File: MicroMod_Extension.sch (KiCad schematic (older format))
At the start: 69 parts, among them J1 2199230-4, J2 XKB_U262-16XN-4BVC11, J3 RSP-122811-01, SW1 TL1014BF160QG, U1 24aa64ft-eot, U2 nRF51822-QFAA-R7, U3 RFX2411N, U4 TPS62170DSG, U5 NCP702SN30T1G, U6 NCP702SN30T1G, Y1 TSX-3225_16.0000MF18X-AC3

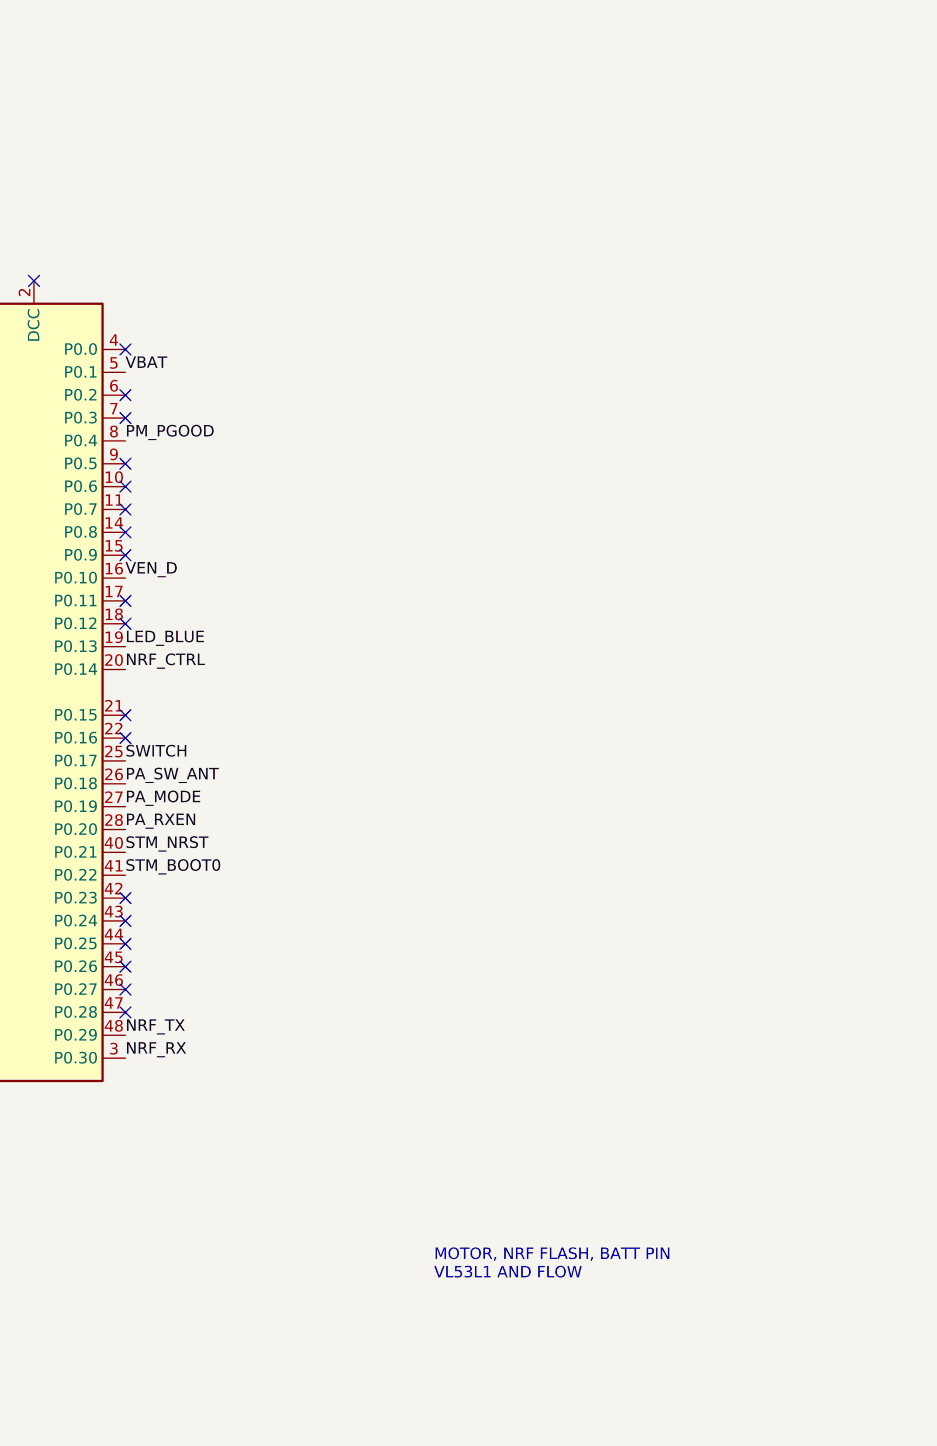
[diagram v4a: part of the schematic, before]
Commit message: add connector for esc and flow
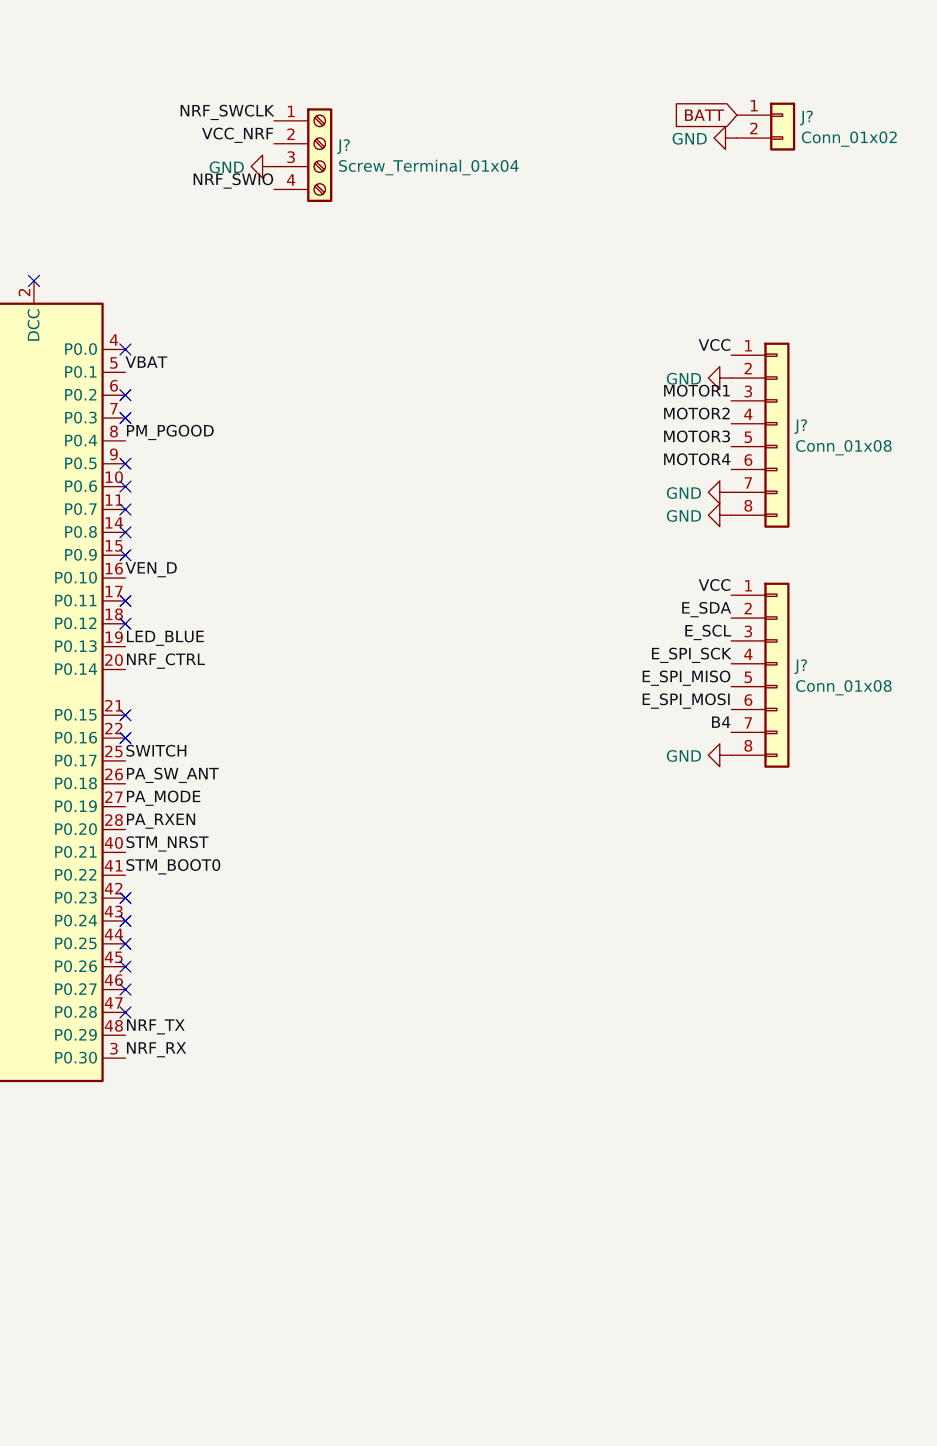
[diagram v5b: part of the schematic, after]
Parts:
- added J?: Screw_Terminal_01x04, Connector_PinHeader_2.54mm:PinHeader_1x04_P2.54mm_Vertical, symbol Connector:Screw_Terminal_01x04
- added J?: Conn_01x02, symbol Connector_Generic:Conn_01x02
- added J? (x2): Conn_01x08, MicroMod_Extension:JST_SUR_BM08B-SURS-TF_1x08-1MP_P0.80mm_Vertical, symbol Connector_Generic:Conn_01x08
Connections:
- net B4: now also J?.7 (Pin_7)
- net BATT: now also J?.1 (Pin_1)
- net E_SCL: now also J?.3 (Pin_3)
- net E_SDA: now also J?.2 (Pin_2)
- net E_SPI_MISO: now also J?.5 (Pin_5)
- net E_SPI_MOSI: now also J?.6 (Pin_6)
- net E_SPI_SCK: now also J?.4 (Pin_4)
- net GND: now also J?.2 (Pin_2), J?.2 (Pin_2), J?.3 (Pin_3), J?.7 (Pin_7), J?.8 (Pin_8), J?.8 (Pin_8)
- net MOTOR1: now also J?.3 (Pin_3)
- net MOTOR2: now also J?.4 (Pin_4)
- net MOTOR3: now also J?.5 (Pin_5)
- net MOTOR4: now also J?.6 (Pin_6)
- net NRF_SWCLK: now also J?.1 (Pin_1)
- net NRF_SWIO: now also J?.4 (Pin_4)
- net VCC: now also J?.1 (Pin_1), J?.1 (Pin_1)
- net VCC_NRF: now also J?.2 (Pin_2)
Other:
- note removed: "MOTOR, NRF FLASH, BATT PIN\nVL53L1 AND FLOW"
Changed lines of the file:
@@
 Text Label 10250 4525 2    50   ~ 0
 NRF_SWCLK
-$Comp
-L MicroMod_Extension:XKB_U262-16XN-4BVC11 J2
-U 1 1 617B133B
-P 1550 7950
-F 0 "J2" H 1583 9125 50  0000 C CNN
-F 1 "XKB_U262-16XN-4BVC11" H 1583 9034 50  0000 C CNN
-F 2 "Connector_USB:USB_C_Receptacle_XKB_U262-16XN-4BVC11" H 1580 7960 50  0001 C CNN
-F 3 "" H 1580 7960 50  0001 C CNN
-	1    1550 7950
-	1    0    0    -1
-$EndComp
-Wire Wire Line
-	2050 8650 2050 8750
 Wire Wire Line
 	2050 9000 1450 9000
-Connection ~ 2050 8750
-Wire Wire Line
-	2050 8750 2050 9000
 Connection ~ 2050 9000
-Connection ~ 2050 8050
-Connection ~ 2050 7800
 Wire Wire Line
 	2050 7200 2050 7300
@@
 Wire Wire Line
 	2150 7300 2050 7300
-Connection ~ 2050 8450
-Connection ~ 2050 7300
 NoConn ~ 2050 8250
 NoConn ~ 2050 8350
@@
 Wire Wire Line
 	2050 7000 2050 7100
-Connection ~ 2050 7000
 $Comp
 L MicroMod_Extension:2450BM14E0003T FL1
@@
 Wire Wire Line
 	2050 7200 2150 7200
-Connection ~ 2050 7200
 NoConn ~ 12050 4825
 NoConn ~ 12050 4725
@@
 	8500 5850 8500 5325
 Connection ~ 8500 5325
-Text Notes 13400 6000 0    50   ~ 0
- MOTOR, NRF FLASH, BATT PIN\nVL53L1 AND FLOW
+Connection ~ 2050 7200
+Connection ~ 2050 7000
+Connection ~ 2050 7300
+Connection ~ 2050 8450
+Connection ~ 2050 7800
+Connection ~ 2050 8050
+Connection ~ 2050 8750
+Wire Wire Line
+	2050 8750 2050 9000
+Wire Wire Line
+	2050 8650 2050 8750
+$Comp
+L MicroMod_Extension:XKB_U262-16XN-4BVC11 J2
+U 1 1 617B133B
+P 1550 7950
+F 0 "J2" H 1583 9125 50  0000 C CNN
+F 1 "XKB_U262-16XN-4BVC11" H 1583 9034 50  0000 C CNN
+F 2 "Connector_USB:USB_C_Receptacle_XKB_U262-16XN-4BVC11" H 1580 7960 50  0001 C CNN
+F 3 "" H 1580 7960 50  0001 C CNN
+	1    1550 7950
+	1    0    0    -1
+$EndComp
+$Comp
+L Connector:Screw_Terminal_01x04 J?
+U 1 1 6180CF84
+P 12900 1025
+F 0 "J?" H 12980 1017 50  0000 L CNN
+F 1 "Screw_Terminal_01x04" H 12980 926 50  0000 L CNN
+F 2 "Connector_PinHeader_2.54mm:PinHeader_1x04_P2.54mm_Vertical" H 12900 1025 50  0001 C CNN
+F 3 "~" H 12900 1025 50  0001 C CNN
+	1    12900 1025
+	1    0    0    -1
+$EndComp
+Text Label 12700 925  2    50   ~ 0
+NRF_SWCLK
+Text Label 12700 1225 2    50   ~ 0
+NRF_SWIO
+Text Label 12700 1025 2    50   ~ 0
+VCC_NRF
+$Comp
+L power:GND #PWR?
+U 1 1 61871AB2
+P 12700 1125
+F 0 "#PWR?" H 12700 875 50  0001 C CNN
+F 1 "GND" V 12705 997 50  0000 R CNN
+F 2 "" H 12700 1125 50  0001 C CNN
+F 3 "" H 12700 1125 50  0001 C CNN
+	1    12700 1125
+	0    1    1    0
+$EndComp
+$Comp
+L Connector_Generic:Conn_01x02 J?
+U 1 1 6189B41D
+P 14925 900
+F 0 "J?" H 15005 892 50  0000 L CNN
+F 1 "Conn_01x02" H 15005 801 50  0000 L CNN
+F 2 "" H 14925 900 50  0001 C CNN
+F 3 "~" H 14925 900 50  0001 C CNN
+	1    14925 900
+	1    0    0    -1
+$EndComp
+$Comp
+L power:GND #PWR?
+U 1 1 6189BE51
+P 14725 1000
+F 0 "#PWR?" H 14725 750 50  0001 C CNN
+F 1 "GND" V 14730 872 50  0000 R CNN
+F 2 "" H 14725 1000 50  0001 C CNN
+F 3 "" H 14725 1000 50  0001 C CNN
+	1    14725 1000
+	0    1    1    0
+$EndComp
+Text GLabel 14725 900  0    50   Input ~ 0
+BATT
+$Comp
+L Connector_Generic:Conn_01x08 J?
+U 1 1 6197BE2D
+P 14900 2250
+F 0 "J?" H 14980 2242 50  0000 L CNN
+F 1 "Conn_01x08" H 14980 2151 50  0000 L CNN
+F 2 "MicroMod_Extension:JST_SUR_BM08B-SURS-TF_1x08-1MP_P0.80mm_Vertical" H 14900 2250 50  0001 C CNN
+F 3 "~" H 14900 2250 50  0001 C CNN
+	1    14900 2250
+	1    0    0    -1
+$EndComp
+$Comp
+L Connector_Generic:Conn_01x08 J?
+U 1 1 6197CCB9
+P 14900 3300
+F 0 "J?" H 14980 3292 50  0000 L CNN
+F 1 "Conn_01x08" H 14980 3201 50  0000 L CNN
+F 2 "MicroMod_Extension:JST_SUR_BM08B-SURS-TF_1x08-1MP_P0.80mm_Vertical" H 14900 3300 50  0001 C CNN
+F 3 "~" H 14900 3300 50  0001 C CNN
+	1    14900 3300
+	1    0    0    -1
+$EndComp
+Text Label 14700 1950 2    50   ~ 0
+VCC
+Text Label 14700 3000 2    50   ~ 0
+VCC
+$Comp
+L power:GND #PWR?
+U 1 1 619F4806
+P 14700 2650
+F 0 "#PWR?" H 14700 2400 50  0001 C CNN
+F 1 "GND" V 14705 2522 50  0000 R CNN
+F 2 "" H 14700 2650 50  0001 C CNN
+F 3 "" H 14700 2650 50  0001 C CNN
+	1    14700 2650
+	0    1    1    0
+$EndComp
+$Comp
+L power:GND #PWR?
+U 1 1 61A085B5
+P 14700 3700
+F 0 "#PWR?" H 14700 3450 50  0001 C CNN
+F 1 "GND" V 14705 3572 50  0000 R CNN
+F 2 "" H 14700 3700 50  0001 C CNN
+F 3 "" H 14700 3700 50  0001 C CNN
+	1    14700 3700
+	0    1    1    0
+$EndComp
+Text Label 14700 2150 2    50   ~ 0
+MOTOR1
+Text Label 14700 2250 2    50   ~ 0
+MOTOR2
+Text Label 14700 2350 2    50   ~ 0
+MOTOR3
+Text Label 14700 2450 2    50   ~ 0
+MOTOR4
+$Comp
+L power:GND #PWR?
+U 1 1 61A7FB45
+P 14700 2550
+F 0 "#PWR?" H 14700 2300 50  0001 C CNN
+F 1 "GND" V 14705 2422 50  0000 R CNN
+F 2 "" H 14700 2550 50  0001 C CNN
+F 3 "" H 14700 2550 50  0001 C CNN
+	1    14700 2550
+	0    1    1    0
+$EndComp
+$Comp
+L power:GND #PWR?
+U 1 1 61A9399D
+P 14700 2050
+F 0 "#PWR?" H 14700 1800 50  0001 C CNN
+F 1 "GND" V 14705 1922 50  0000 R CNN
+F 2 "" H 14700 2050 50  0001 C CNN
+F 3 "" H 14700 2050 50  0001 C CNN
+	1    14700 2050
+	0    1    1    0
+$EndComp
+Text Label 14700 3100 2    50   ~ 0
+E_SDA
+Text Label 14700 3200 2    50   ~ 0
+E_SCL
+Text Label 14700 3300 2    50   ~ 0
+E_SPI_SCK
+Text Label 14700 3400 2    50   ~ 0
+E_SPI_MISO
+Text Label 14700 3500 2    50   ~ 0
+E_SPI_MOSI
+Text Label 14700 3600 2    50   ~ 0
+B4
 $EndSCHEMATC

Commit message: update pcb
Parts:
- added J8, J9: Conn_01x04, MicroMod_Extension:JST_SUR_BM04B-SURS-TF_1x04-1MP_P0.80mm_Vertical, symbol Connector_Generic:Conn_01x04
- J7: renamed from J?; footprint (none) -> Connector_PinHeader_2.54mm:PinHeader_1x02_P2.54mm_Vertical
- U8: renamed from U?; footprint (none) -> MicroMod_Extension:PQFN45P200X200X100-10N
- gave numbers to parts that had none: 9
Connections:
- net BATT: now also J5.1 (Pin_1), J5.2 (Pin_2)
- net E_RX1: now also J8.2 (Pin_2)
- net E_RX2: now also J9.2 (Pin_2)
- net E_TX1: now also J8.3 (Pin_3)
- net E_TX2: now also J9.3 (Pin_3)
- net GND: now also J4.4 (Pin_4), J8.4 (Pin_4), J9.4 (Pin_4); no longer J4.3 (Pin_3), J5.2 (Pin_2)
- net NRF_SWCLK: now also J4.2 (Pin_2); no longer J4.1 (Pin_1)
- net NRF_SWIO: now also J4.3 (Pin_3); no longer J4.4 (Pin_4)
- net OTG_FS_D+: now also J2.A6 (D+), J2.B6 (D+); no longer J2.A7 (D-), J2.B7 (D-)
- net OTG_FS_D-: now also J2.A7 (D-), J2.B7 (D-); no longer J2.A6 (D+), J2.B6 (D+)
- net VCC: now also J8.1 (Pin_1), J9.1 (Pin_1); no longer J5.1 (Pin_1)
- net VCC_NRF: now also J4.1 (Pin_1); no longer J4.2 (Pin_2)
- net at FL1.3 (BALANCED_PORT1): now also U2.32 (ANT2); no longer U2.31 (ANT1)
- net at FL1.4 (BALANCED_PORT2): now also U2.31 (ANT1); no longer U2.32 (ANT2)
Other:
- note added: "Connector"
- moved on the sheet: C1, C10, C12, C13, C18, C19, C20, C21, C22, C23, C24, C25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

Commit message: update
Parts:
- added J10: 2199230-4, MicroMod_Extension:M.2-CARD-E-22, symbol MicroMod_Extension:2199230-4
- added TP4, TP5, TP6, TP7: TestPoint, TestPoint:TestPoint_Plated_Hole_D3.0mm, symbol Connector:TestPoint
- added TP8: TestPoint, MicroMod_Extension:97730256330R, symbol Connector:TestPoint
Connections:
- net GND: now also TP4.1, TP5.1, TP6.1, TP7.1, TP8.1
- new net: J10.S1 (SHIELD), J10.S2 (SHIELD)
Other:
- moved on the sheet: J7
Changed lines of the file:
@@
 L Connector_Generic:Conn_01x02 J7
 U 1 1 6189B41D
-P 15425 975
-F 0 "J7" H 15505 967 50  0000 L CNN
-F 1 "Conn_01x02" H 15505 876 50  0000 L CNN
-F 2 "Connector_PinHeader_2.54mm:PinHeader_1x02_P2.54mm_Vertical" H 15425 975 50  0001 C CNN
-F 3 "~" H 15425 975 50  0001 C CNN
-	1    15425 975
+P 15400 750
+F 0 "J7" H 15480 742 50  0000 L CNN
+F 1 "Conn_01x02" H 15480 651 50  0000 L CNN
+F 2 "Connector_PinHeader_2.54mm:PinHeader_1x02_P2.54mm_Vertical" H 15400 750 50  0001 C CNN
+F 3 "~" H 15400 750 50  0001 C CNN
+	1    15400 750
 	1    0    0    -1
 $EndComp
@@
 L power:GND #PWR0134
 U 1 1 6189BE51
-P 15225 1075
-F 0 "#PWR0134" H 15225 825 50  0001 C CNN
-F 1 "GND" V 15230 947 50  0000 R CNN
-F 2 "" H 15225 1075 50  0001 C CNN
-F 3 "" H 15225 1075 50  0001 C CNN
-	1    15225 1075
-	0    1    1    0
-$EndComp
-Text GLabel 15225 975  0    50   Input ~ 0
+P 15200 850
+F 0 "#PWR0134" H 15200 600 50  0001 C CNN
+F 1 "GND" V 15205 722 50  0000 R CNN
+F 2 "" H 15200 850 50  0001 C CNN
+F 3 "" H 15200 850 50  0001 C CNN
+	1    15200 850
+	0    1    1    0
+$EndComp
+Text GLabel 15200 750  0    50   Input ~ 0
 BATT
 $Comp
@@
 Wire Wire Line
 	10175 2225 10250 2225
+$Comp
+L Connector:TestPoint TP4
+U 1 1 6181E613
+P 14925 1200
+F 0 "TP4" H 14983 1318 50  0000 L CNN
+F 1 "TestPoint" H 14983 1227 50  0000 L CNN
+F 2 "TestPoint:TestPoint_Plated_Hole_D3.0mm" H 15125 1200 50  0001 C CNN
+F 3 "~" H 15125 1200 50  0001 C CNN
+	1    14925 1200
+	1    0    0    -1
+$EndComp
+$Comp
+L Connector:TestPoint TP5
+U 1 1 6181F914
+P 15150 1200
+F 0 "TP5" H 15208 1318 50  0000 L CNN
+F 1 "TestPoint" H 15208 1227 50  0000 L CNN
+F 2 "TestPoint:TestPoint_Plated_Hole_D3.0mm" H 15350 1200 50  0001 C CNN
+F 3 "~" H 15350 1200 50  0001 C CNN
+	1    15150 1200
+	1    0    0    -1
+$EndComp
+$Comp
+L Connector:TestPoint TP6
+U 1 1 6183323A
+P 15350 1200
+F 0 "TP6" H 15408 1318 50  0000 L CNN
+F 1 "TestPoint" H 15408 1227 50  0000 L CNN
+F 2 "TestPoint:TestPoint_Plated_Hole_D3.0mm" H 15550 1200 50  0001 C CNN
+F 3 "~" H 15550 1200 50  0001 C CNN
+	1    15350 1200
+	1    0    0    -1
+$EndComp
+$Comp
+L Connector:TestPoint TP7
+U 1 1 618469A4
+P 15575 1200
+F 0 "TP7" H 15633 1318 50  0000 L CNN
+F 1 "TestPoint" H 15633 1227 50  0000 L CNN
+F 2 "TestPoint:TestPoint_Plated_Hole_D3.0mm" H 15775 1200 50  0001 C CNN
+F 3 "~" H 15775 1200 50  0001 C CNN
+	1    15575 1200
+	1    0    0    -1
+$EndComp
+Wire Wire Line
+	14925 1200 15150 1200
+Connection ~ 15150 1200
+Wire Wire Line
+	15150 1200 15350 1200
+Connection ~ 15350 1200
+Wire Wire Line
+	15350 1200 15575 1200
+$Comp
+L power:GND #PWR0140
+U 1 1 6186E42C
+P 15150 1200
+F 0 "#PWR0140" H 15150 950 50  0001 C CNN
+F 1 "GND" V 15155 1072 50  0000 R CNN
+F 2 "" H 15150 1200 50  0001 C CNN
+F 3 "" H 15150 1200 50  0001 C CNN
+	1    15150 1200
+	1    0    0    -1
+$EndComp
+$Comp
+L MicroMod_Extension:2199230-4 J10
+U 1 1 61980F5E
+P 13625 3700
+F 0 "J10" H 13625 5767 50  0000 C CNN
+F 1 "2199230-4" H 13625 5676 50  0000 C CNN
+F 2 "MicroMod_Extension:M.2-CARD-E-22" H 13625 3700 50  0001 L BNN
+F 3 "" H 13625 3700 50  0001 L BNN
+F 4 "Compliant" H 13625 3700 50  0001 L BNN "EU_RoHS_Compliance"
+F 5 "2199230-4" H 13625 3700 50  0001 L BNN "Comment"
+	1    13625 3700
+	1    0    0    -1
+$EndComp
+$Comp
+L Connector:TestPoint TP8
+U 1 1 6199C5E3
+P 14775 1200
+F 0 "TP8" H 14833 1318 50  0000 L CNN
+F 1 "TestPoint" H 14833 1227 50  0000 L CNN
+F 2 "MicroMod_Extension:97730256330R" H 14975 1200 50  0001 C CNN
+F 3 "~" H 14975 1200 50  0001 C CNN
+	1    14775 1200
+	1    0    0    -1
+$EndComp
+Wire Wire Line
+	14775 1200 14925 1200
+Connection ~ 14925 1200
 $EndSCHEMATC
